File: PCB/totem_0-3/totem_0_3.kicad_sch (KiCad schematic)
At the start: 100 parts, among them J1 MJ-4PP-9, J2 MJ-4PP-9, J3 Conn_01x12_Socket, J4 Conn_01x03_Socket, J5 Conn_01x03_Socket, SW1 SW_Push_45deg, SW10 SW_Push_45deg, SW11 SW_Push_45deg, SW12 SW_Push_45deg, SW13 SW_Push_45deg, SW14 SW_Push_45deg, SW15 SW_Push_45deg, SW16 SW_Push_45deg, SW17 SW_Push_45deg, SW18 SW_Push_45deg, SW19 SW_Push_45deg, SW2 SW_Push_45deg, SW20 SW_Push, SW21 SW_SPDT, SW22 SW_SPDT, SW23 SW_Push, SW24 SW_Push_45deg, SW25 SW_Push_45deg, SW26 SW_Push_45deg, SW27 SW_Push_45deg, SW28 SW_Push_45deg, SW29 SW_Push_45deg, SW3 SW_Push_45deg, SW30 SW_Push_45deg, SW31 SW_Push_45deg, SW32 SW_Push_45deg, SW33 SW_Push_45deg, SW34 SW_Push_45deg, SW35 SW_Push_45deg, SW36 SW_Push_45deg, SW37 SW_Push_45deg, SW38 SW_Push_45deg, SW39 SW_Push_45deg, SW4 SW_Push_45deg, SW40 SW_Push_45deg, SW41 SW_Push_45deg, SW42 SW_Push_45deg, SW5 SW_Push_45deg, SW6 SW_Push_45deg, SW7 SW_Push_45deg, SW8 SW_Push_45deg, SW9 SW_Push_45deg, U1 xiao-ble, U2 74HC595, U3 xiao-ble, U4 74HC595

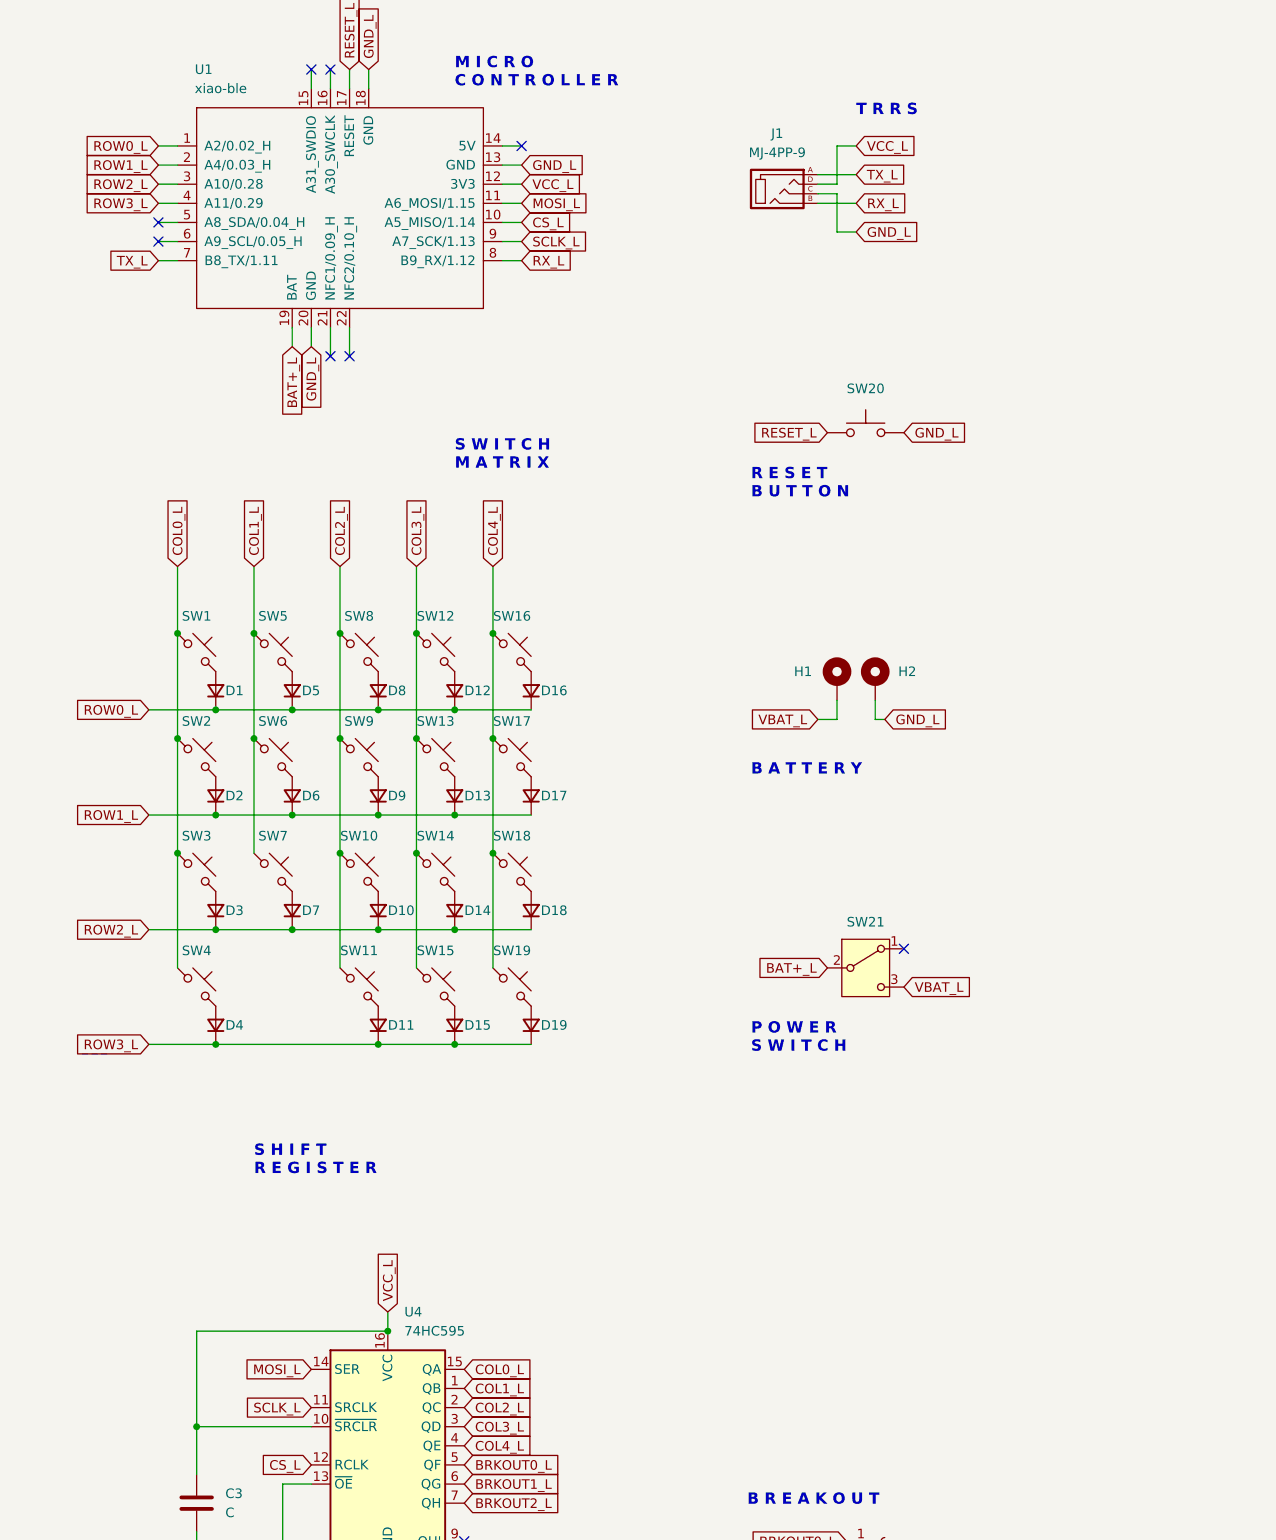
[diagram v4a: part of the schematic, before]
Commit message: sch: add i2c breakout
Signed-off-by: Anant Thazhemadam <anant.thazhemadam@gmail.com>
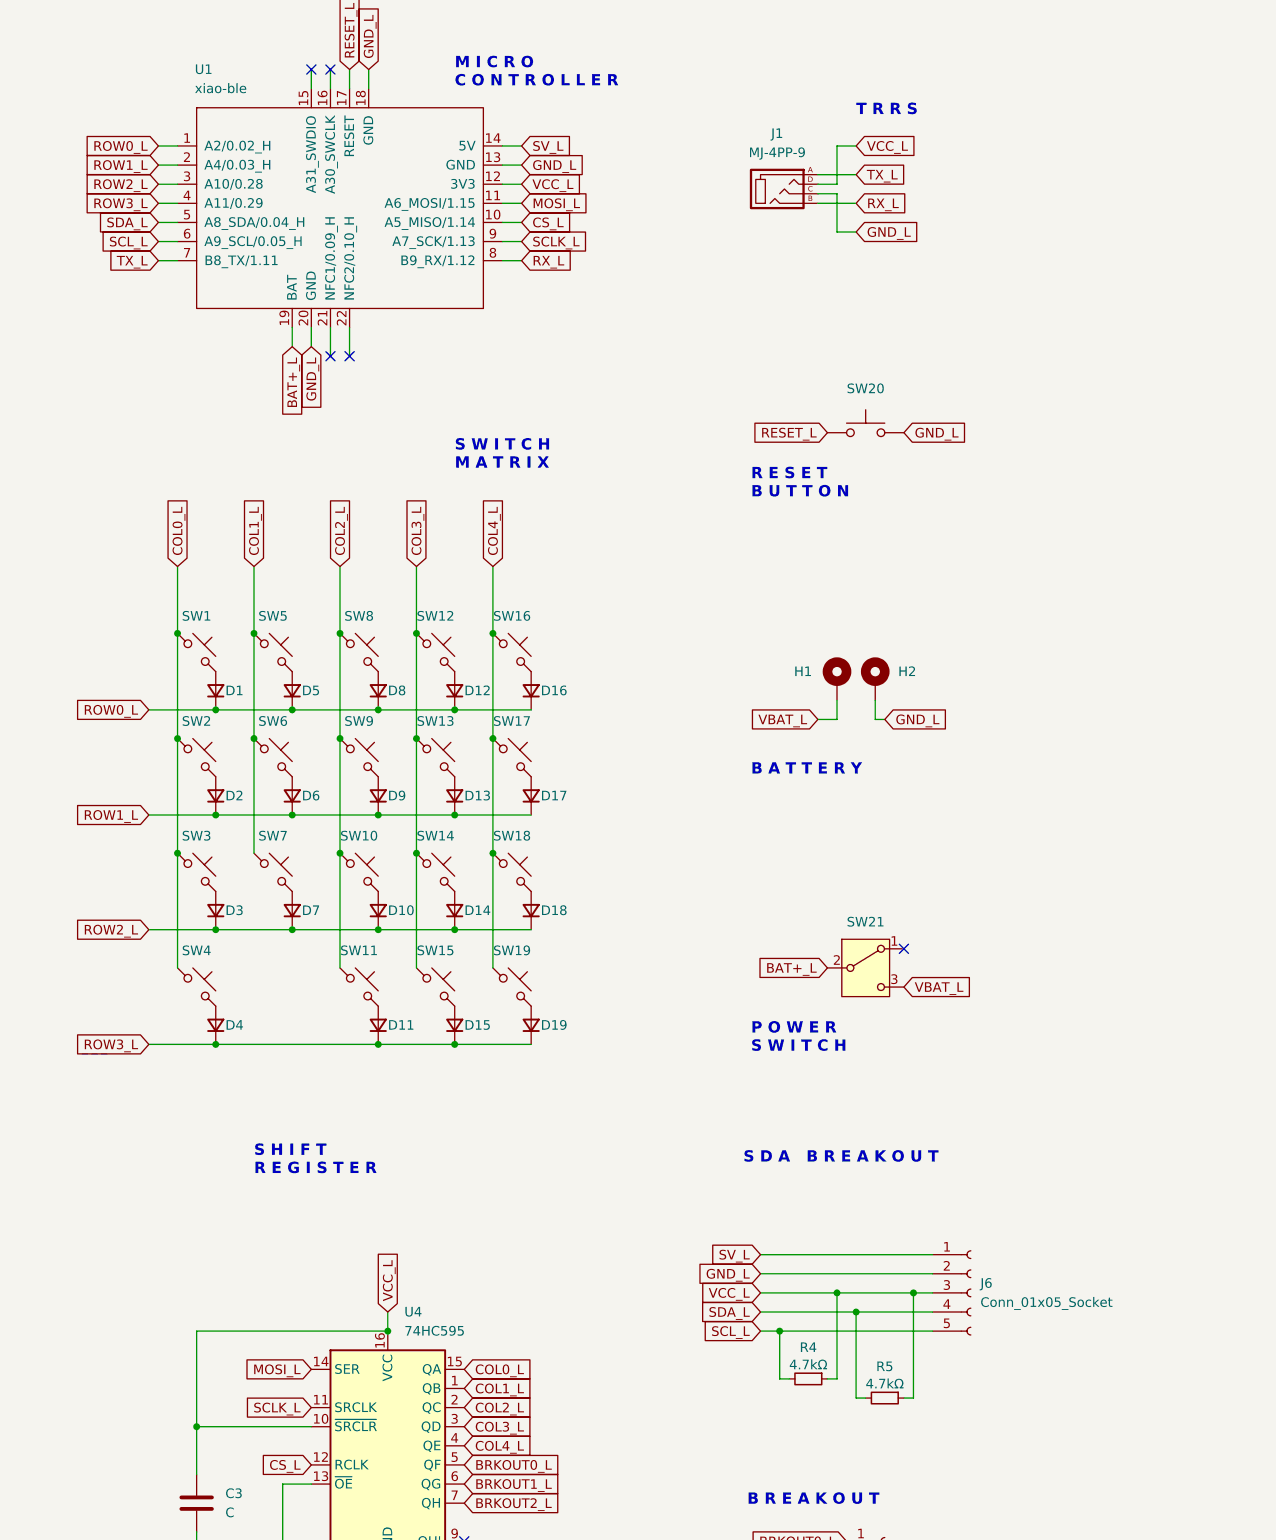
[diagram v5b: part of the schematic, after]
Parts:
- added J6: Conn_01x05_Socket, Connector_PinHeader_2.54mm:PinHeader_1x05_P2.54mm_Vertical, symbol Connector:Conn_01x05_Socket
- added R4, R5: 4.7kΩ, Resistor_SMD:R_0805_2012Metric_Pad1.20x1.40mm_HandSolder, symbol Device:R_Small
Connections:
- net GND_L: now also J6.2 (Pin_2)
- net VCC_L: now also J6.3 (Pin_3), R4.1, R5.1
- net SV_L: now reaches U1.14 (5V)
- net SV_L: now also J6.1 (Pin_1)
- net SDA_L: now reaches U1.5 (A8_SDA/0.04_H)
- net SDA_L: now also J6.4 (Pin_4), R5.2
- net SCL_L: now reaches U1.6 (A9_SCL/0.05_H)
- net SCL_L: now also J6.5 (Pin_5), R4.2
- no-connect marks 23 -> 20
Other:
- note added: "S D A B R E A K O U T"

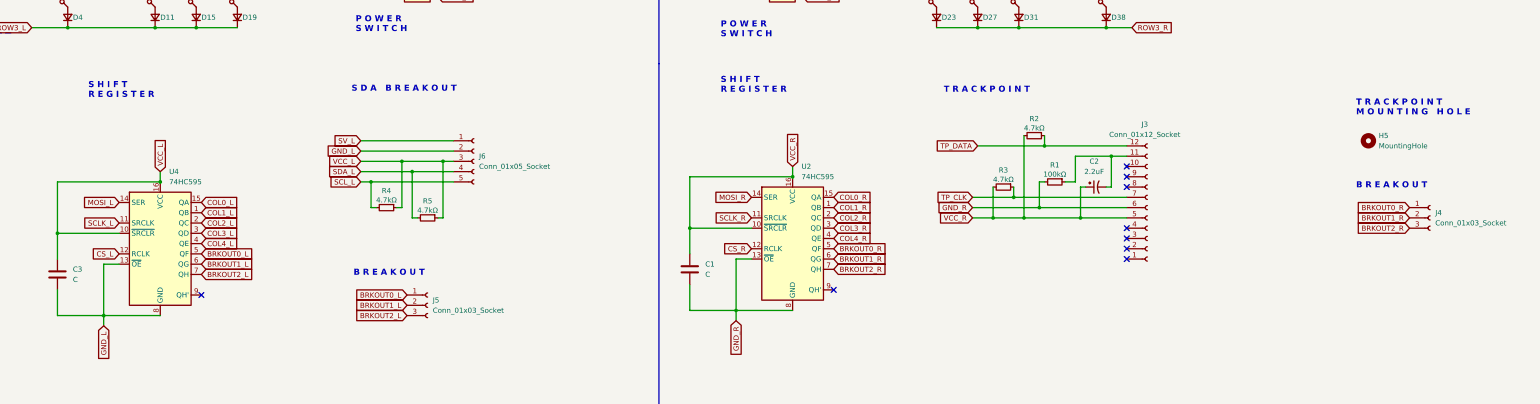
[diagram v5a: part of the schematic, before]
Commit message: sch: fix typo, realign, specify C value
Signed-off-by: Anant Thazhemadam <anant.thazhemadam@gmail.com>
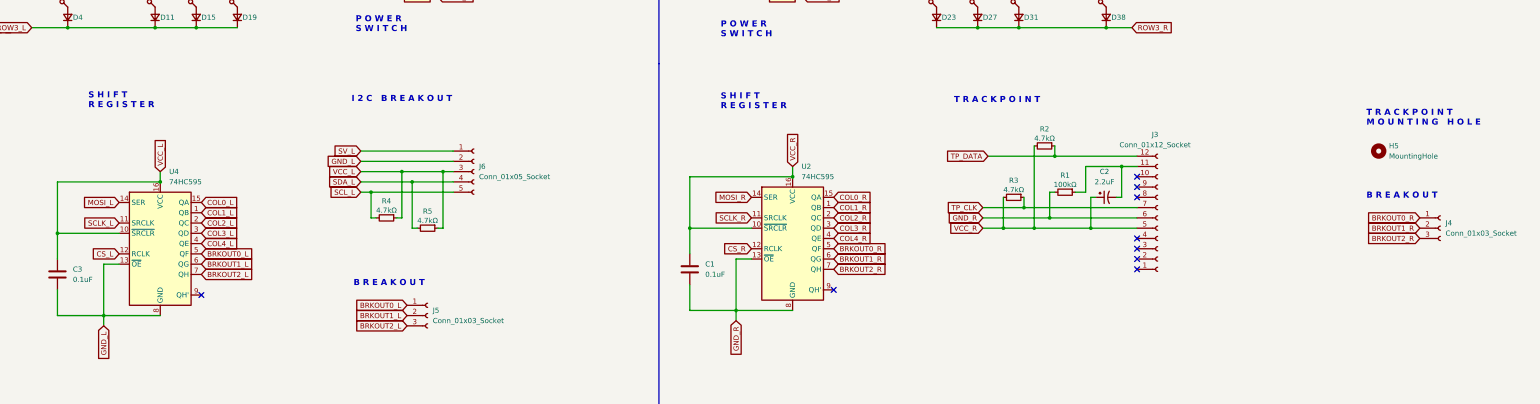
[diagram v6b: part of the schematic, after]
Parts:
- C1, C3: value C -> 0.1uF
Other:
- note added: "I 2 C B R E A K O U T"
- note removed: "S D A B R E A K O U T"
- moved on the sheet: C2, H5, J3, J4, J5, J6, R1, R2, R3, R4, R5

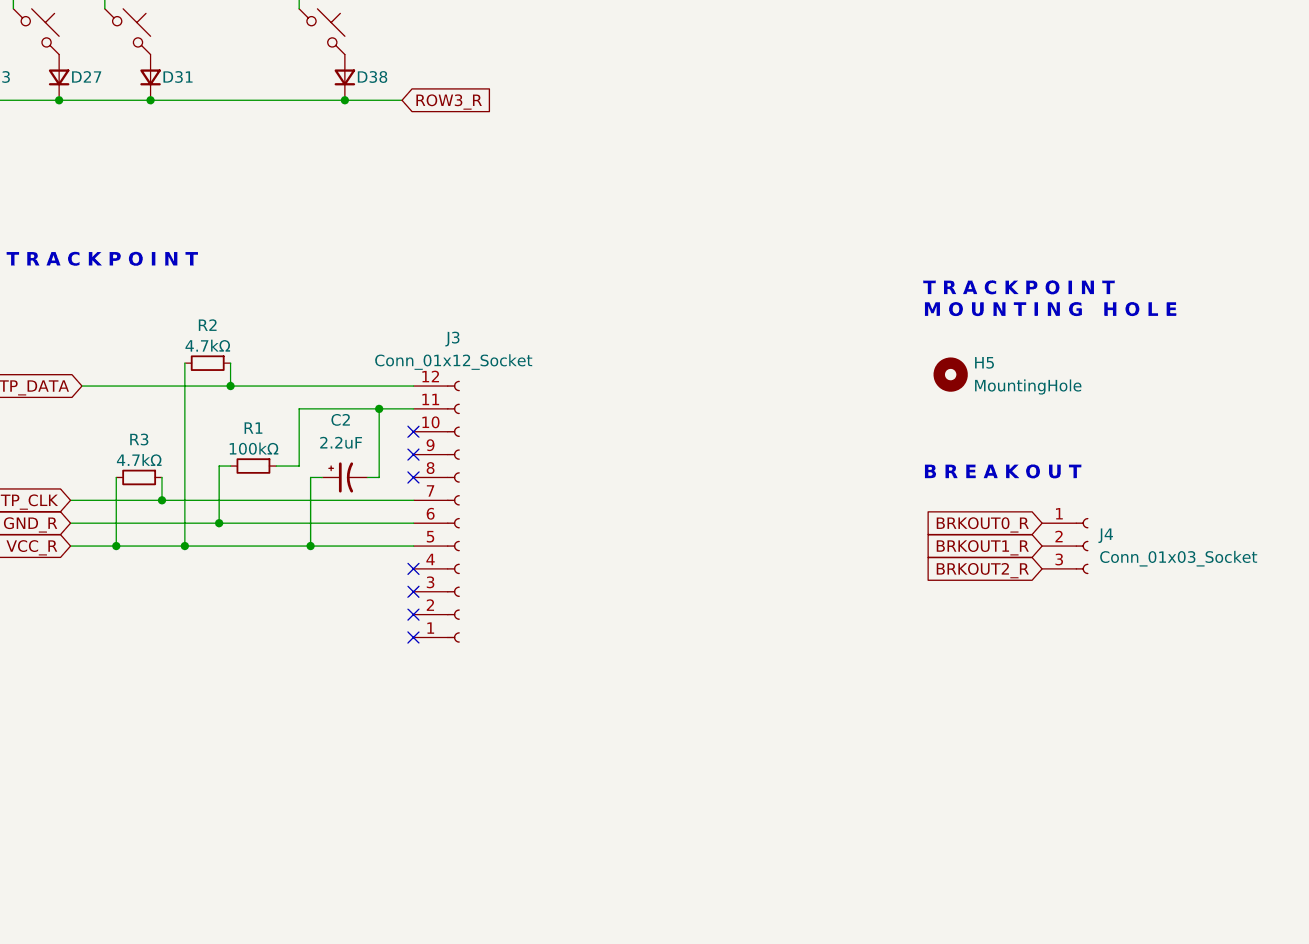
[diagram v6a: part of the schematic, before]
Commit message: pcb: add breakout for trackpoint
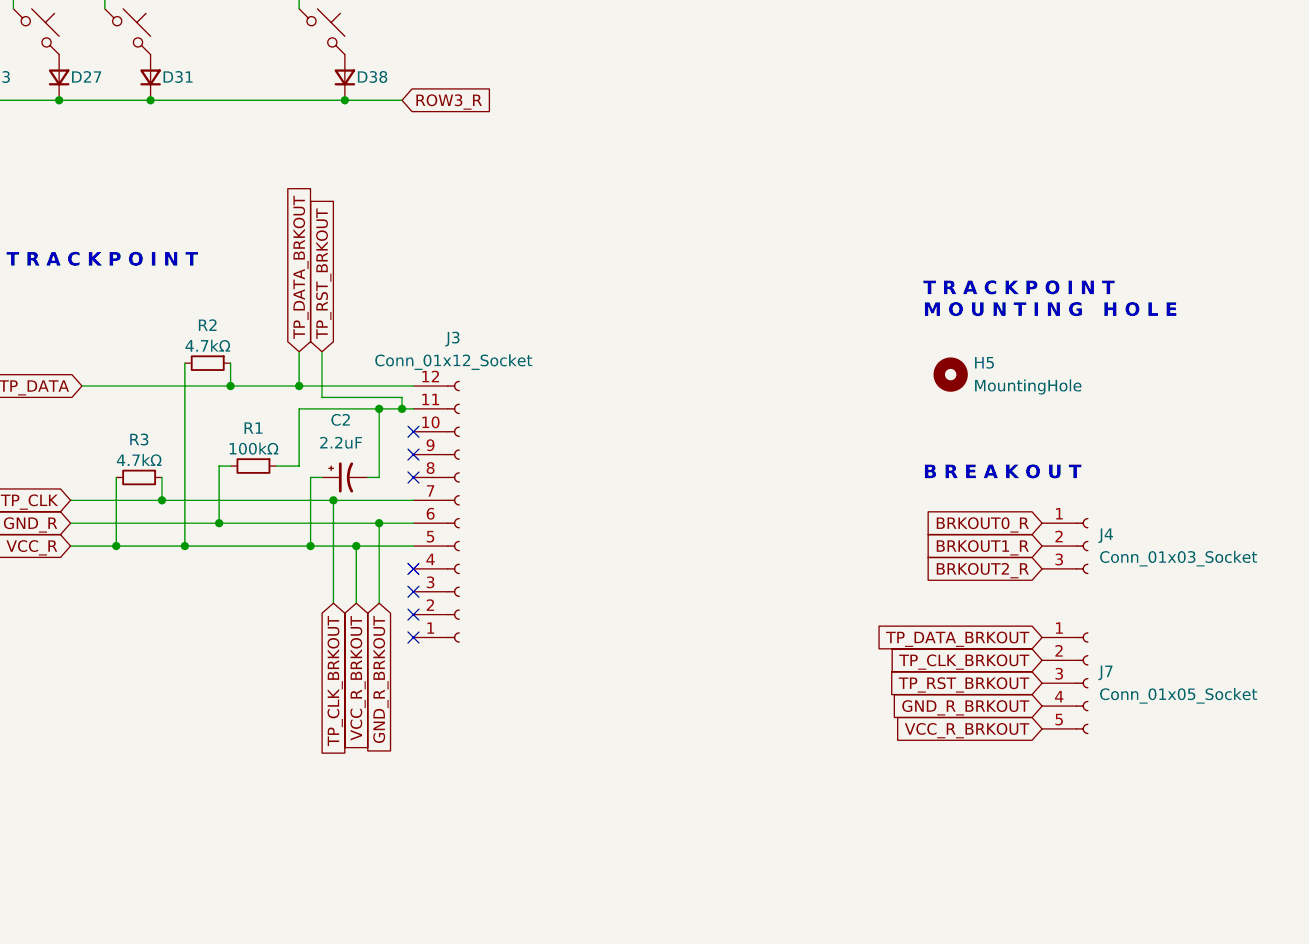
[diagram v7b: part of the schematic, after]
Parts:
- added J7: Conn_01x05_Socket, Connector_PinHeader_2.54mm:PinHeader_1x05_P2.54mm_Vertical, symbol Connector:Conn_01x05_Socket
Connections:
- net GND_R: now also J7.4 (Pin_4)
- net TP_CLK: now also J7.2 (Pin_2)
- net TP_DATA: now also J7.1 (Pin_1)
- net VCC_R: now also J7.5 (Pin_5)
- net TP_RST_BRKOUT: now reaches C2.2, J3.11 (Pin_11), R1.1
- net TP_RST_BRKOUT: now also J7.3 (Pin_3)
